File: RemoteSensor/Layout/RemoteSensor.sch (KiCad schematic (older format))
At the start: 55 parts, among them J1 PRG_HEADER, J2 LCD_HEADER, J3 USB_B_Micro, J4 BATT_CONN, Q1 2N7002, Q3 2N7002, SW1 BTN_RST, SW2 BTN_LOAD, SW3 SW_DPDT_x2, U1 ESP-12F, U2 74LVC2G02, U3 LM50CIM3, U4 MCP73831-2-OT, U5 LM3670MF, U6 BD48ExxG, U7 BD48ExxG

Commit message: Move circuits on different sheets
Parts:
- removed C1, C5, C?: 1u, Capacitor_SMD:C_0603_1608Metric_Pad1.05x0.95mm_HandSolder, symbol Device:C
- removed C2, C6, C?: 0.1u, Capacitor_SMD:C_0603_1608Metric_Pad1.05x0.95mm_HandSolder, symbol Device:C
- removed C3, C?: 4.7u, Capacitor_SMD:C_0603_1608Metric_Pad1.05x0.95mm_HandSolder, symbol Device:C
- removed C4, C?: 10u, Capacitor_SMD:C_0603_1608Metric_Pad1.05x0.95mm_HandSolder, symbol Device:C
- removed D1: HB_LED, LED_SMD:LED_0603_1608Metric_Pad1.05x0.95mm_HandSolder, symbol Device:LED
- removed D2: BATT_LED, LED_SMD:LED_0603_1608Metric_Pad1.05x0.95mm_HandSolder, symbol Device:LED
- removed J1: PRG_HEADER, Connector_PinSocket_2.54mm:PinSocket_1x03_P2.54mm_Vertical, symbol Connector_Generic:Conn_01x03
- removed J2: LCD_HEADER, Connector_PinHeader_2.54mm:PinHeader_1x04_P2.54mm_Vertical, symbol Connector_Generic:Conn_01x04
- removed J3: USB_B_Micro, Connector_USB:USB_Micro-B_Molex_47346-0001, symbol Connector:USB_B_Micro
- removed J4: BATT_CONN, Connector_JST:JST_PH_S2B-PH-SM4-TB_1x02-1MP_P2.00mm_Horizontal, symbol Connector:Conn_01x02_Male
- removed L1, L?: 2.2u, Inductor_SMD:L_0603_1608Metric_Pad1.05x0.95mm_HandSolder, symbol Device:L
- removed Q1, Q3, Q?: 2N7002, digikey-footprints:SOT-23-3, symbol dk_Transistors-FETs-MOSFETs-Single:2N7002
- removed R1, R13, R14, R15, R16, R2, R3, R4, R7: 10k, Resistor_SMD:R_0603_1608Metric_Pad1.05x0.95mm_HandSolder, symbol Device:R_US
- removed R10, R11: 1k, Resistor_SMD:R_0603_1608Metric_Pad1.05x0.95mm_HandSolder, symbol Device:R_US
- removed R12: 2k, Resistor_SMD:R_0603_1608Metric_Pad1.05x0.95mm_HandSolder, symbol Device:R_US
- removed R5, R6: 4.7k, Resistor_SMD:R_0603_1608Metric_Pad1.05x0.95mm_HandSolder, symbol Device:R_US
- removed R8, R9: 100, Resistor_SMD:R_0603_1608Metric_Pad1.05x0.95mm_HandSolder, symbol Device:R_US
- removed R? (x2): 10k, symbol Device:R_US
- removed S1: NAV_SWITCH, NAV_SWITCH, symbol SparkFun-Switches:NAV_SWITCH
- removed SW1: BTN_RST, Button_Switch_SMD:SW_SPST_TL3342, symbol Switch:SW_Push
- removed SW2: BTN_LOAD, Button_Switch_SMD:SW_SPST_TL3342, symbol Switch:SW_Push
- removed SW3: SW_DPDT_x2, Switches:SWITCH_DPDT_SMD_AYZ0202, symbol Switch:SW_DPDT_x2
- removed U1: ESP-12F, RF_Module:ESP-12E, symbol RF_Module:ESP-12F
- removed U2: 74LVC2G02, Package_SO:VSSOP-8_2.3x2mm_P0.5mm, symbol 74xGxx:74LVC2G02
- removed U3: LM50CIM3, SOT95P260X110-3N, symbol LM50CIM3:LM50CIM3
- removed U4: MCP73831-2-OT, Package_TO_SOT_SMD:SOT-23-5, symbol Battery_Management:MCP73831-2-OT
- removed U5, U?: LM3670MF, Package_TO_SOT_SMD:TSOT-23-5, symbol Regulator_Switching:LM3670MF
- removed U6, U7: BD48ExxG, Package_TO_SOT_SMD:SOT-23-5, symbol Power_Management:BD48ExxG
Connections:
- net labels removed: 3.3V, BATT_PIN, BATT_STS, CENTER_PIN, CHARGER_STS, CHARGE_STS, DOWN_PIN, HB_PIN, PRG_RX, PRG_TX, RADIO_RX, RADIO_TX, RST, SCL, SDA, SLEEP_PIN, SLEEP_STS, TEMP_PIN, UP_PIN, V_BATT, V_USB, WAKE_STS
- wire segments 183 -> 4
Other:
- moved on the sheet: H1, H2, H3, H4

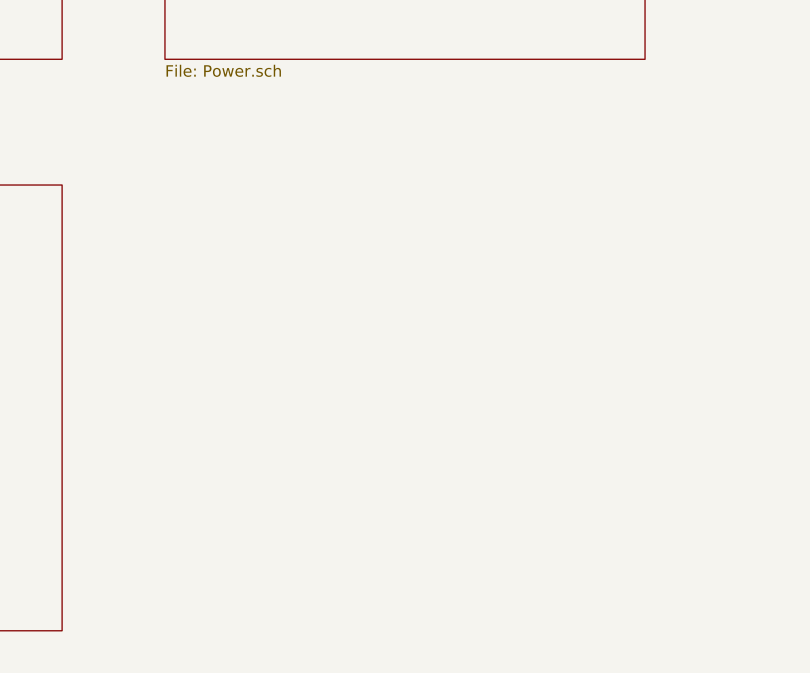
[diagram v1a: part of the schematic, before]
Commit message: Add FTDI USB to serial
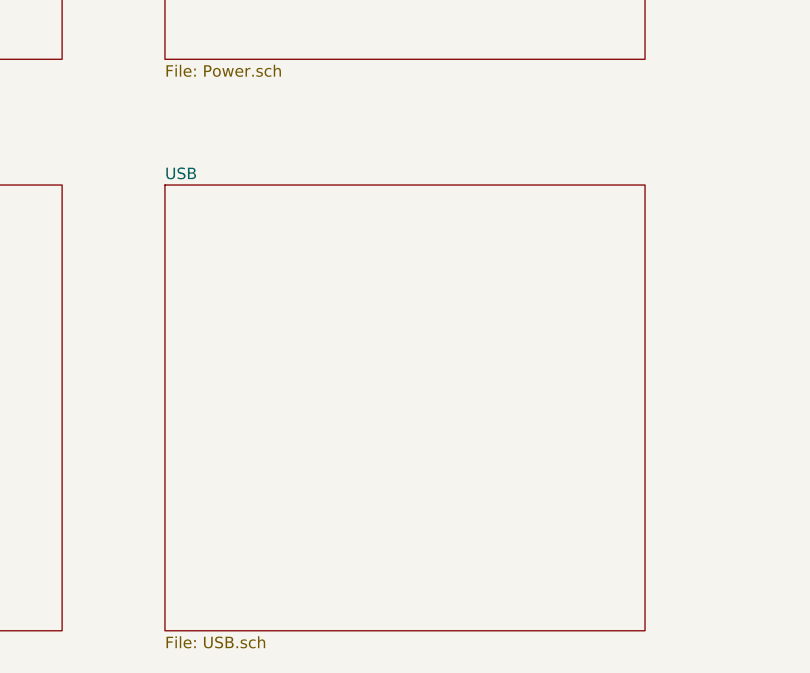
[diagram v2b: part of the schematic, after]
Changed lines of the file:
@@
 $Descr USLetter 11000 8500
 encoding utf-8
-Sheet 1 4
+Sheet 1 5
 Title ""
 Date ""
@@
 F1 "Processor.sch" 50
 $EndSheet
+$Sheet
+S 3950 4000 2100 1950
+U 5EF070B6
+F0 "USB" 50
+F1 "USB.sch" 50
+$EndSheet
 $EndSCHEMATC

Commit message: Update sensor schematic
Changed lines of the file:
@@
 EESchema Schematic File Version 4
-LIBS:RemoteSensor-cache
-EELAYER 29 0
+EELAYER 30 0
 EELAYER END
 $Descr USLetter 11000 8500
@@
 	7150 4200 7700 4200
 $Comp
-L SparkFun-PowerSymbols:GND #GND0118
+L RemoteSensor-rescue:GND-SparkFun-PowerSymbols #GND0118
 U 1 1 5ED93B1B
 P 7700 3850
@@
 	7700 3850 8200 3850
 $Comp
-L SparkFun-PowerSymbols:GND #GND0119
+L RemoteSensor-rescue:GND-SparkFun-PowerSymbols #GND0119
 U 1 1 5ED940BC
 P 7700 4200

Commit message: Change what pins are used for i2c
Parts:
- H1, H2, H3, H4: symbol Mechanical:MountingHole_Pad -> RemoteSensor-rescue:MountingHole_Pad-Mechanical
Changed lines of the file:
@@
 $EndDescr
 $Comp
-L Mechanical:MountingHole_Pad H2
+L RemoteSensor-rescue:MountingHole_Pad-Mechanical H2
 U 1 1 5ED8175C
 P 7150 4100
@@
 $EndComp
 $Comp
-L Mechanical:MountingHole_Pad H1
+L RemoteSensor-rescue:MountingHole_Pad-Mechanical H1
 U 1 1 5ED820A4
 P 7150 3750
@@
 $EndComp
 $Comp
-L Mechanical:MountingHole_Pad H3
+L RemoteSensor-rescue:MountingHole_Pad-Mechanical H3
 U 1 1 5ED83464
 P 8200 3750
@@
 $EndComp
 $Comp
-L Mechanical:MountingHole_Pad H4
+L RemoteSensor-rescue:MountingHole_Pad-Mechanical H4
 U 1 1 5ED84C2B
 P 8200 4100
